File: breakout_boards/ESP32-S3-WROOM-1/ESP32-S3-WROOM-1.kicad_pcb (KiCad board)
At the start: 2 copper layers, 57.4 x 50.3 mm, 47 parts, among them J1 USB_C_Receptacle_USB2.0_16P, J2 JST-XH 6 pin, J4 JST-XH 6 pin, SW1 SW_Push, SW2 SW_Push, U1 ESP32-S3-WROOM-1, U2 AP7361-33E

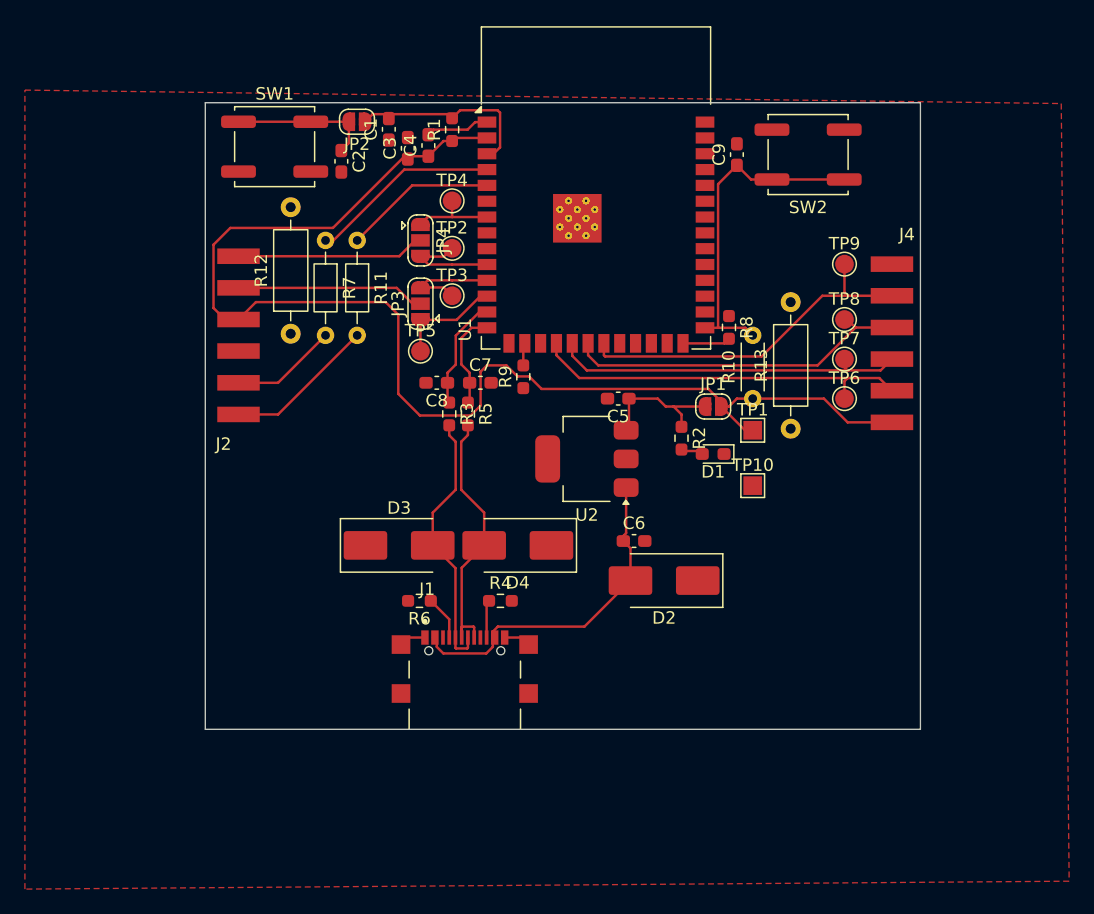
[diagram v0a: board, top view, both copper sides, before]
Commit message: Fixed ESP32-WROOM breakout board
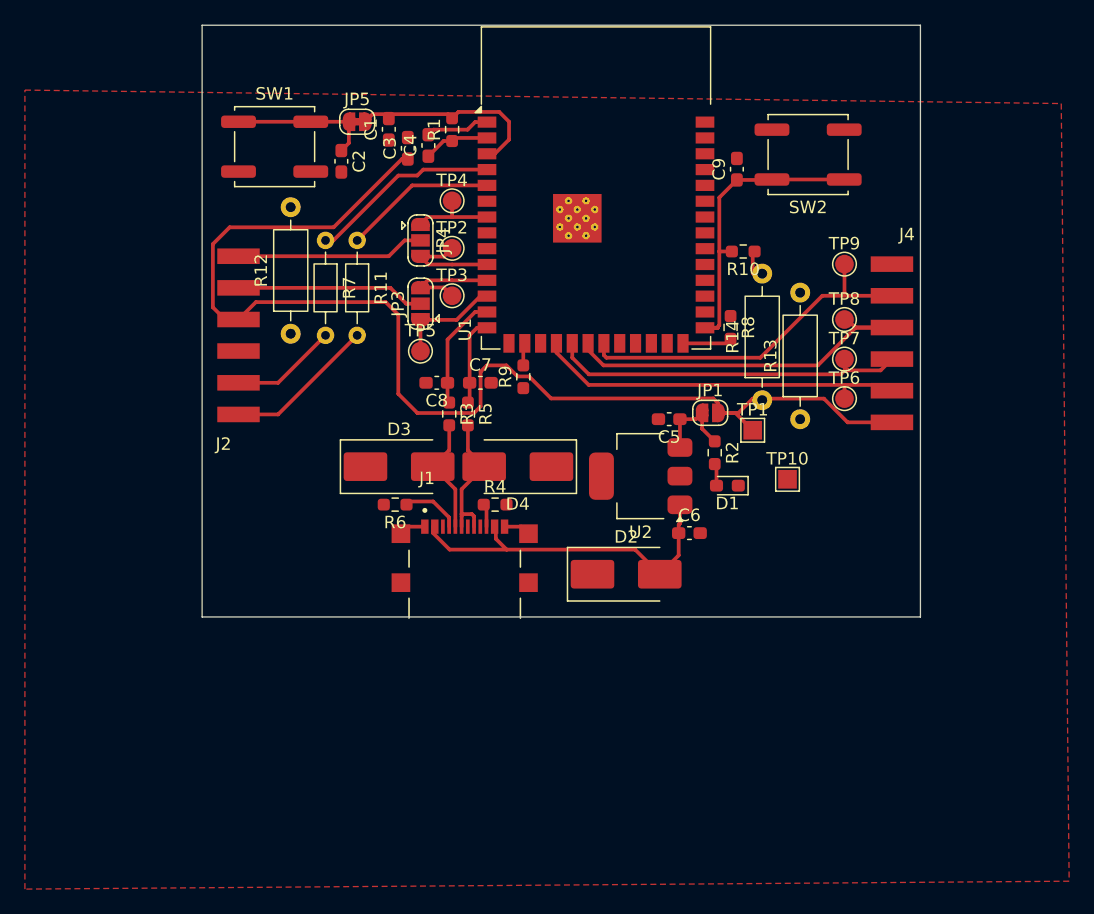
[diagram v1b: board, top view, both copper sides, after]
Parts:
- removed JP2: SolderJumper_2_Open, Jumper:SolderJumper-2_P1.3mm_Open_RoundedPad1.0x1.5mm
- added JP5: SolderJumper_2_Bridged, Jumper:SolderJumper-2_P1.3mm_Bridged_RoundedPad1.0x1.5mm, F.Cu at (115.6, 72.4)
- added R14: Bridge (0Ω), Resistor_THT:R_Axial_DIN0207_L6.3mm_D2.5mm_P10.16mm_Horizontal, F.Cu at (148.1, 94.7)
- R10: footprint Resistor_THT:R_Axial_DIN0204_L3.6mm_D1.6mm_P5.08mm_Horizontal -> Resistor_SMD:R_0603_1608Metric_Pad0.98x0.95mm_HandSolder
- moved R10 11.8 mm to (146.6, 82.8), turned to 180 degrees
- moved J1 8.90 mm to (124.2, 108.6)
- moved R6 7.97 mm to (118.6, 103.1)
- moved R4 7.74 mm to (126.6, 103.1)
- moved D3 6.32 mm to (118.9, 100.1)
- moved D4 6.32 mm to (128.5, 100.1)
- moved U2 4.53 mm to (138.3, 100.8)
- moved C6 4.49 mm to (142.2, 105.4)
- moved C5 4.41 mm to (140.6, 96.3)
- moved D2 3.09 mm to (137.2, 108.7), turned to 0 degrees
- moved R2 2.91 mm to (144.3, 99.0)
- moved TP10 2.84 mm to (150.1, 101.1)
- moved D1 2.79 mm to (145.3, 101.6)
- moved C9 1.17 mm to (146.1, 76.2)
- moved R13 1.08 mm to (151.1, 96.3)
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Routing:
- net /USB_RAW_DN: track 21.5 -> 9.44 mm
- net /USB_RAW_DP: track 21.5 -> 11.3 mm
- net Net-(JP1-A): track 10.9 -> 6.97 mm
- net /SPI2_CLK: track 28.1 -> 30.8 mm
- net /GPIO0: track 26.8 -> 24.2 mm
- net Net-(J1-CC1): track 3.55 -> 4.80 mm
- net Net-(J1-CC2): track 3.02 -> 1.86 mm
- net /USB_DP: track 7.91 -> 7.10 mm
- net /SPI2_CS: track 30.8 -> 30.0 mm
- net /EN: track 15.6 -> 16.2 mm
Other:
- board size 57.4 x 50.3 mm -> 57.7 x 47.5 mm

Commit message: Fixed traces and did stuff
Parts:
- moved R6 2.88 mm to (121.5, 103.1)
- moved TP9 2.54 mm to (154.7, 86.4)
- moved TP4 1.90 mm to (123.2, 80.6)
- moved TP8 0.64 mm to (154.7, 88.9)
- moved TP2 0.64 mm to (123.2, 83.2)
- moved TP3 0.64 mm to (123.2, 85.7)
- moved TP6 0.63 mm to (154.7, 94.0)
- moved C1 0.43 mm to (118.1, 72.6)
- moved R1 0.41 mm to (123.2, 72.6)
- moved C3 0.23 mm to (119.6, 74.3)
- moved R4 0.22 mm to (126.9, 103.1)
- moved TP5 0.06 mm to (120.7, 90.8)
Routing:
- net /SPI2_CLK: track 30.8 -> 26.9 mm
- net GND: track 9.13 -> 12.9 mm
- net /USB_RAW_DN: track 9.44 -> 12.3 mm
- net Net-(J1-CC1): track 4.80 -> 1.99 mm
- net /TXD1: track 8.42 -> 5.62 mm
- net /RXD1: track 8.39 -> 5.60 mm
- net /SPI2_MISO: track 28.9 -> 26.2 mm
- net +3.3V: track 102.7 -> 104.5 mm
- net /SPI2_MOSI: track 28.9 -> 27.2 mm
- net /I2C_SDA: track 6.88 -> 5.60 mm
- net /SPI2_CS: track 30.0 -> 28.9 mm
- net Net-(J2-Pin_2): track 8.56 -> 9.39 mm
- net /EN: track 16.2 -> 15.4 mm
- net /GNSS_INT: track 12.2 -> 13.0 mm
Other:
- board text added: "3V3"
- board text added: "CLK"
- board text added: "CS"
- board text added: "GND"
- board text added: "INT"
- board text added: "MISO"
- board text added: "MOSI"
- board text added: "RST"
- board text added: "RX/SCL"
- board text added: "SCL"
- board text added: "SDA"
- board text added: "TX/SDA"

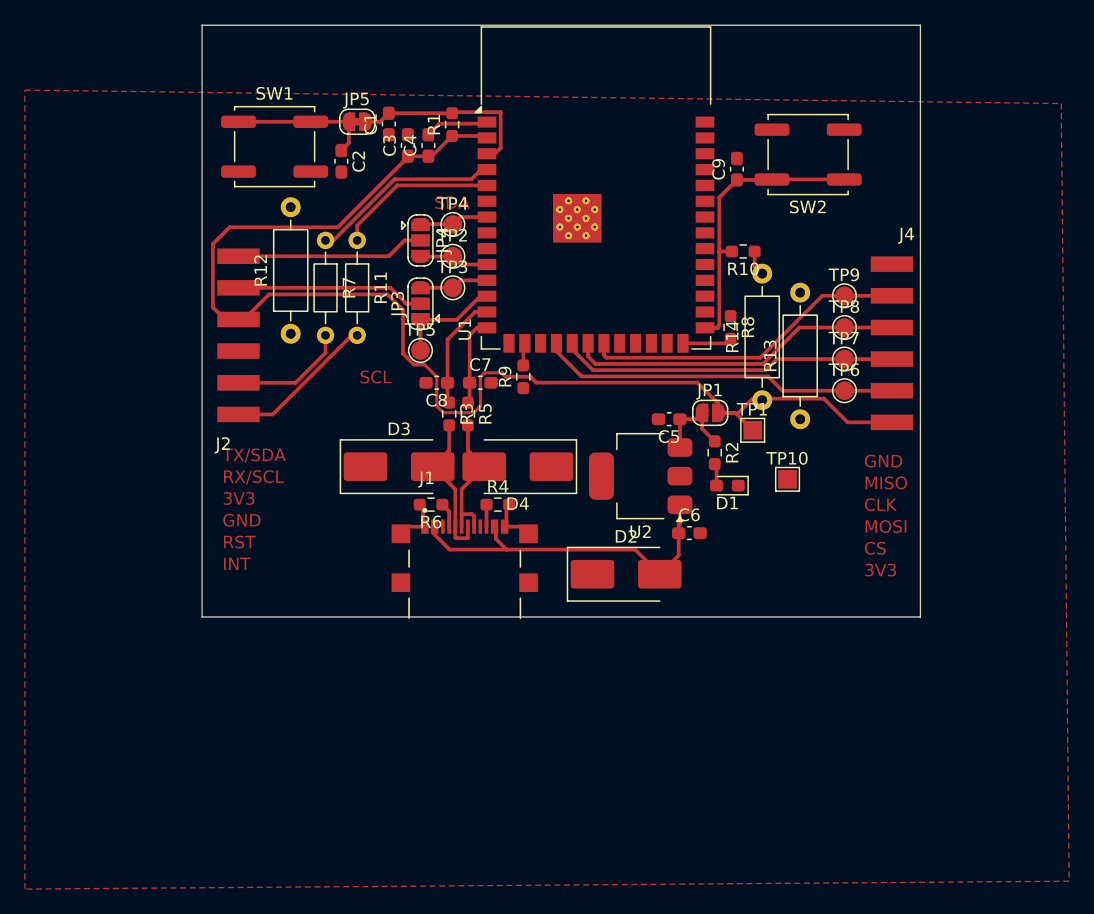
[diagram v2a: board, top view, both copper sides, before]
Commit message: changed edgecuts
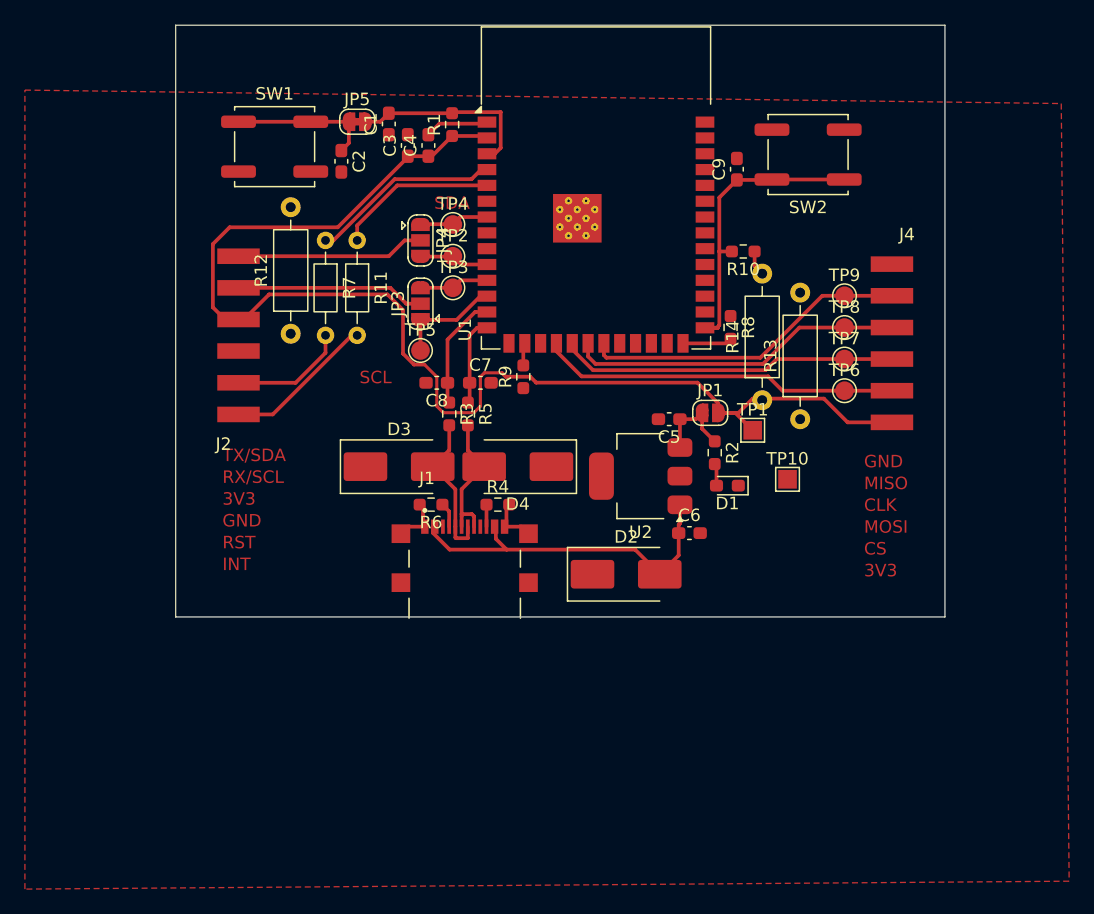
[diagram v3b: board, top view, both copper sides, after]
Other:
- board size 57.7 x 47.5 mm -> 61.8 x 47.5 mm
